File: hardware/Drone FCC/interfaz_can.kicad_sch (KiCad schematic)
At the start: 14 parts, among them J801 CAN 1 Connector 1, J803 CAN 2 Connector 1, U801 SN65HVD230, U802 SN65HVD230

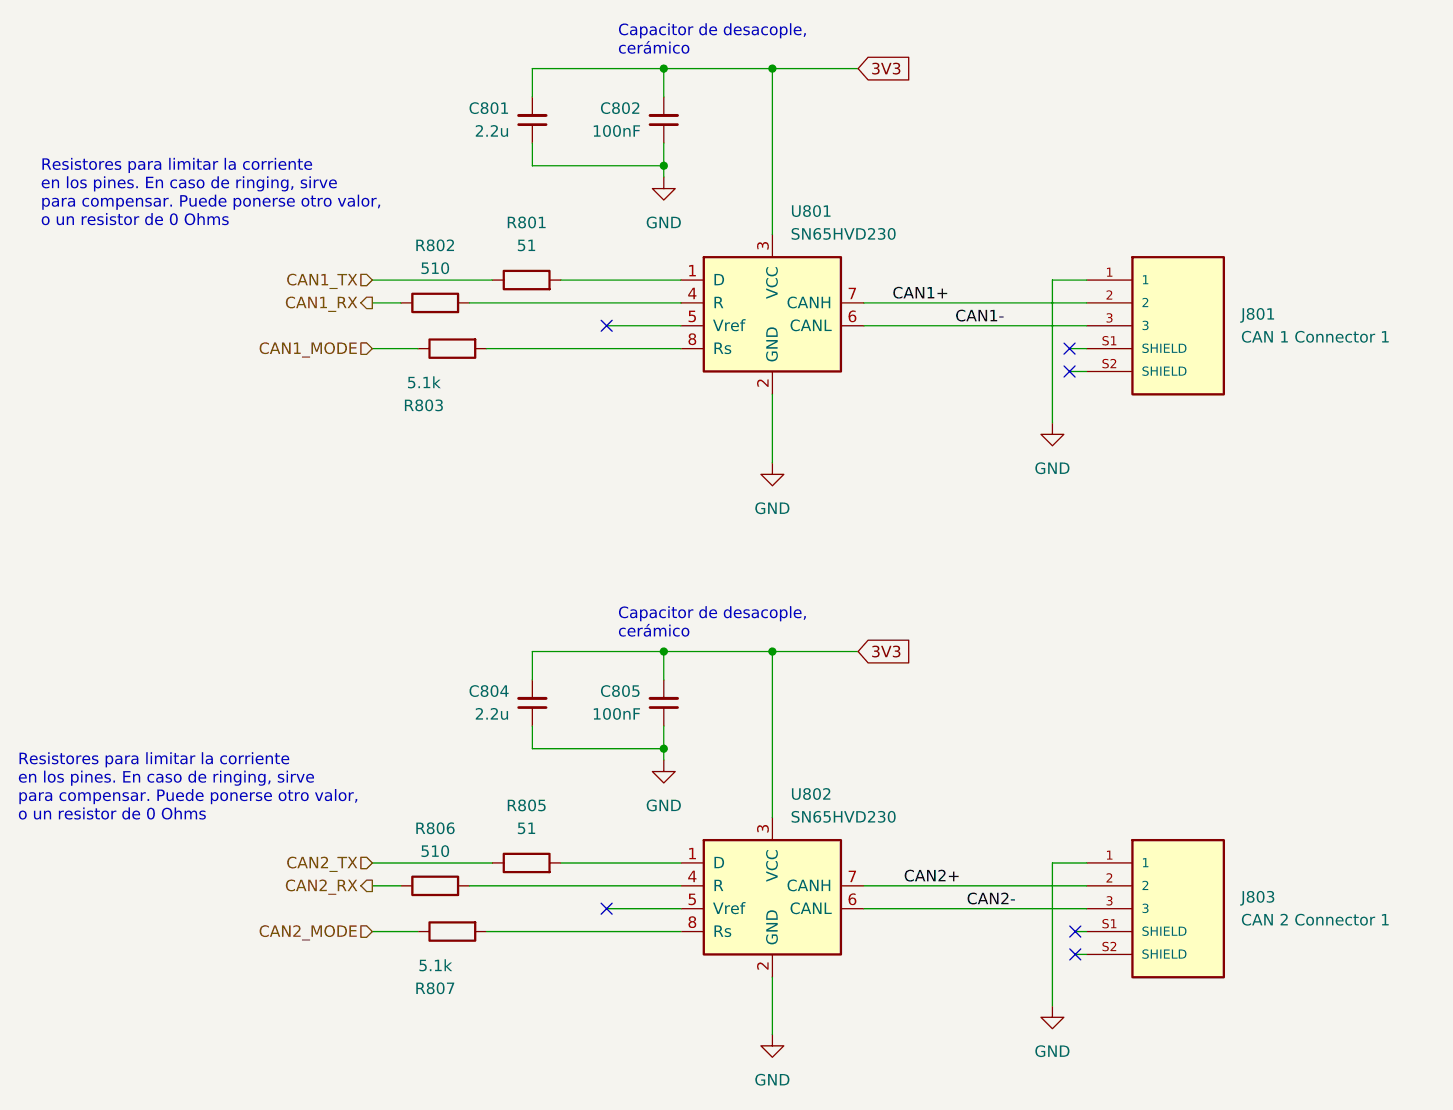
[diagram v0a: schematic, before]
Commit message: re enumeation of componentes
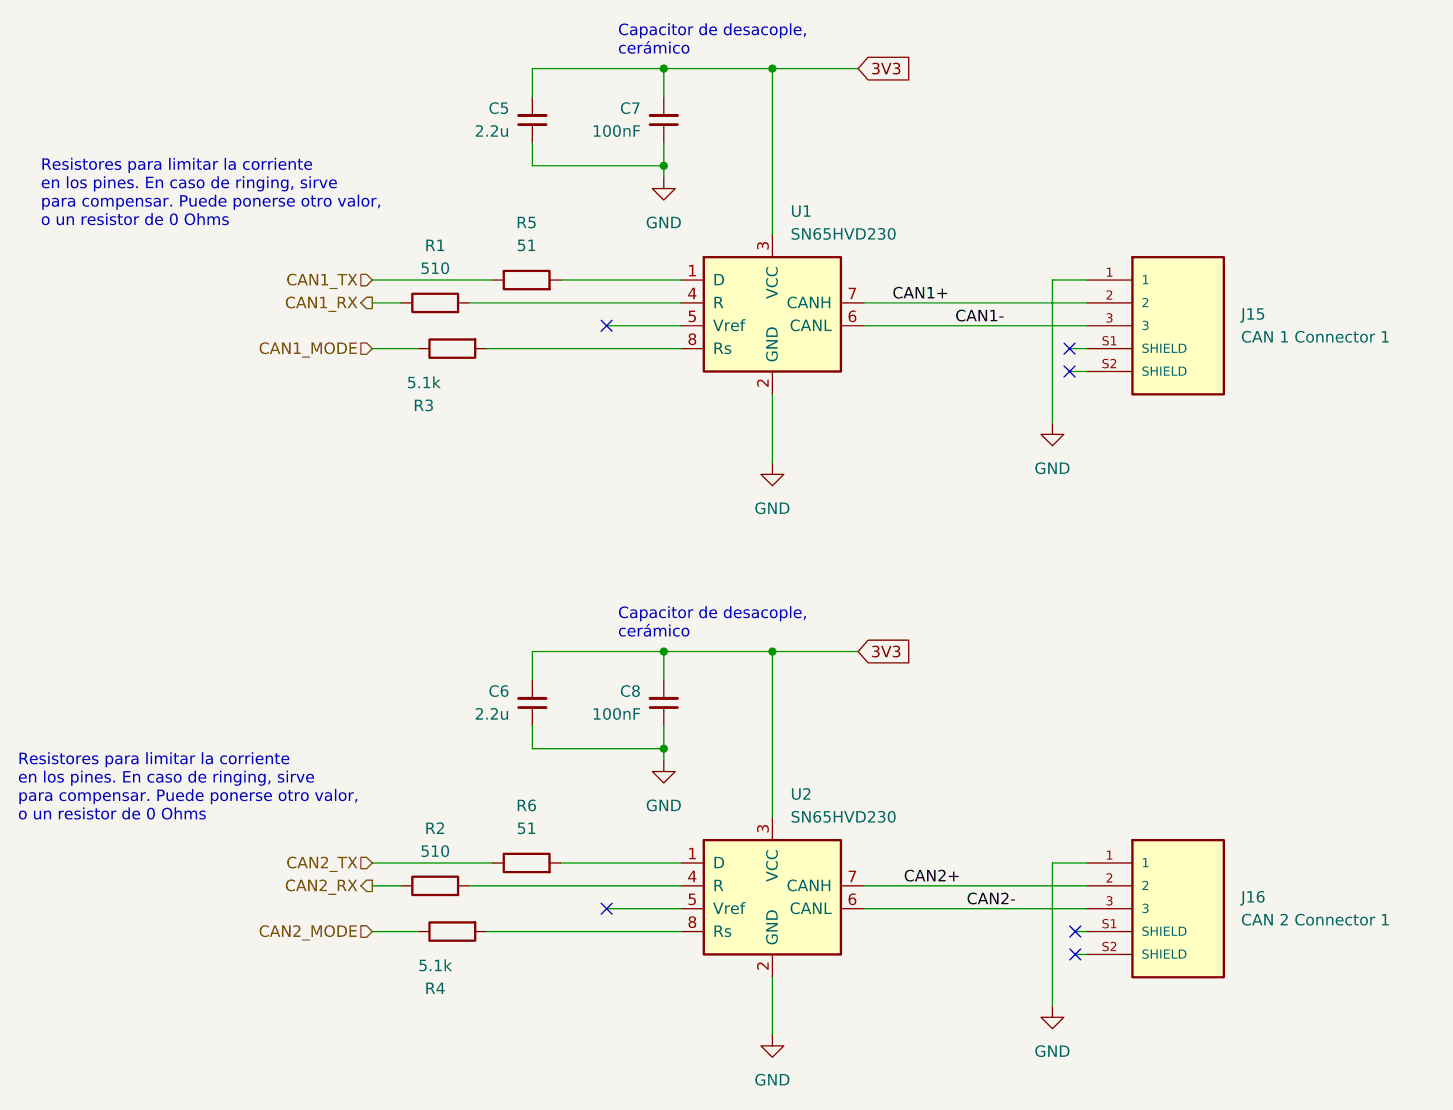
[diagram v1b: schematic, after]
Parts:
- renumbered C801 to C5, C804 to C6, C802 to C7, C805 to C8, J801 to J15, J803 to J16, R802 to R1, R806 to R2, R803 to R3, R807 to R4, R801 to R5, R805 to R6, U801 to U1, U802 to U2
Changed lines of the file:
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@@
   (symbol (lib_id "Device:R") (at 118.11 114.3 90) (unit 1)
     (in_bom yes) (on_board yes) (fields_autoplaced)
-    (property "Reference" "R805" (id 0) (at 118.11 107.95 90))
+    (property "Reference" "R6" (id 0) (at 118.11 107.95 90))
     (property "Value" "51" (id 1) (at 118.11 110.49 90))
     (property "Footprint" "Resistor_SMD:R_0402_1005Metric_Pad0.72x0.64mm_HandSolder" (id 2) (at 118.11 116.078 90)
@@
   (symbol (lib_id "Interface_CAN_LIN:SN65HVD230") (at 145.415 52.07 0) (unit 1)
     (in_bom yes) (on_board yes) (fields_autoplaced)
-    (property "Reference" "U801" (id 0) (at 147.4344 41.91 0)
+    (property "Reference" "U1" (id 0) (at 147.4344 41.91 0)
       (effects (font (size 1.27 1.27)) (justify left))
     )
@@
   (symbol (lib_name "GND_2") (lib_id "power:GND") (at 176.53 130.175 0) (unit 1)
     (in_bom yes) (on_board yes) (fields_autoplaced)
-    (property "Reference" "#PWR0104" (id 0) (at 176.53 136.525 0)
+    (property "Reference" "#PWR024" (id 0) (at 176.53 136.525 0)
       (effects (font (size 1.27 1.27)) hide)
     )
@@
   (symbol (lib_id "DF13A-3P-1.25H(21):HRS_DF13A-3P-1.25H(21)") (at 189.23 137.16 0) (unit 1)
     (in_bom yes) (on_board yes) (fields_autoplaced)
-    (property "Reference" "J803" (id 0) (at 197.485 118.1099 0)
+    (property "Reference" "J16" (id 0) (at 197.485 118.1099 0)
       (effects (font (size 1.27 1.27)) (justify left))
     )
@@
   (symbol (lib_id "Interface_CAN_LIN:SN65HVD230") (at 145.415 116.84 0) (unit 1)
     (in_bom yes) (on_board yes) (fields_autoplaced)
-    (property "Reference" "U802" (id 0) (at 147.4344 106.68 0)
+    (property "Reference" "U2" (id 0) (at 147.4344 106.68 0)
       (effects (font (size 1.27 1.27)) (justify left))
     )
@@
   (symbol (lib_id "Device:R") (at 107.95 52.07 90) (unit 1)
     (in_bom yes) (on_board yes) (fields_autoplaced)
-    (property "Reference" "R802" (id 0) (at 107.95 45.72 90))
+    (property "Reference" "R1" (id 0) (at 107.95 45.72 90))
     (property "Value" "510" (id 1) (at 107.95 48.26 90))
     (property "Footprint" "Resistor_SMD:R_0402_1005Metric_Pad0.72x0.64mm_HandSolder" (id 2) (at 107.95 53.848 90)
@@
   (symbol (lib_id "Device:C_Small") (at 118.745 96.52 0) (mirror x) (unit 1)
     (in_bom yes) (on_board yes) (fields_autoplaced)
-    (property "Reference" "C804" (id 0) (at 116.205 95.2435 0)
+    (property "Reference" "C6" (id 0) (at 116.205 95.2435 0)
       (effects (font (size 1.27 1.27)) (justify right))
     )
@@
   (symbol (lib_id "Device:C_Small") (at 133.35 31.75 0) (mirror x) (unit 1)
     (in_bom yes) (on_board yes) (fields_autoplaced)
-    (property "Reference" "C802" (id 0) (at 130.81 30.4735 0)
+    (property "Reference" "C7" (id 0) (at 130.81 30.4735 0)
       (effects (font (size 1.27 1.27)) (justify right))
     )
@@
   (symbol (lib_id "Device:R") (at 109.855 121.92 90) (mirror x) (unit 1)
     (in_bom yes) (on_board yes)
-    (property "Reference" "R807" (id 0) (at 107.95 128.27 90))
+    (property "Reference" "R4" (id 0) (at 107.95 128.27 90))
     (property "Value" "5.1k" (id 1) (at 107.95 125.73 90))
     (property "Footprint" "Resistor_SMD:R_0402_1005Metric_Pad0.72x0.64mm_HandSolder" (id 2) (at 109.855 120.142 90)
@@
   (symbol (lib_id "Device:C_Small") (at 118.745 31.75 0) (mirror x) (unit 1)
     (in_bom yes) (on_board yes) (fields_autoplaced)
-    (property "Reference" "C801" (id 0) (at 116.205 30.4735 0)
+    (property "Reference" "C5" (id 0) (at 116.205 30.4735 0)
       (effects (font (size 1.27 1.27)) (justify right))
     )
@@
   (symbol (lib_id "Device:R") (at 109.855 57.15 90) (mirror x) (unit 1)
     (in_bom yes) (on_board yes)
-    (property "Reference" "R803" (id 0) (at 106.68 63.5 90))
+    (property "Reference" "R3" (id 0) (at 106.68 63.5 90))
     (property "Value" "5.1k" (id 1) (at 106.68 60.96 90))
     (property "Footprint" "Resistor_SMD:R_0402_1005Metric_Pad0.72x0.64mm_HandSolder" (id 2) (at 109.855 55.372 90)
@@
   (symbol (lib_id "Device:R") (at 107.95 116.84 90) (unit 1)
     (in_bom yes) (on_board yes) (fields_autoplaced)
-    (property "Reference" "R806" (id 0) (at 107.95 110.49 90))
+    (property "Reference" "R2" (id 0) (at 107.95 110.49 90))
     (property "Value" "510" (id 1) (at 107.95 113.03 90))
     (property "Footprint" "Resistor_SMD:R_0402_1005Metric_Pad0.72x0.64mm_HandSolder" (id 2) (at 107.95 118.618 90)
@@
   (symbol (lib_id "power:GND") (at 145.415 69.85 0) (unit 1)
     (in_bom yes) (on_board yes) (fields_autoplaced)
-    (property "Reference" "#PWR0102" (id 0) (at 145.415 76.2 0)
+    (property "Reference" "#PWR021" (id 0) (at 145.415 76.2 0)
       (effects (font (size 1.27 1.27)) hide)
     )
@@
   (symbol (lib_id "Device:C_Small") (at 133.35 96.52 0) (mirror x) (unit 1)
     (in_bom yes) (on_board yes) (fields_autoplaced)
-    (property "Reference" "C805" (id 0) (at 130.81 95.2435 0)
+    (property "Reference" "C8" (id 0) (at 130.81 95.2435 0)
       (effects (font (size 1.27 1.27)) (justify right))
     )
@@
   (symbol (lib_name "GND_2") (lib_id "power:GND") (at 176.53 65.405 0) (unit 1)
     (in_bom yes) (on_board yes) (fields_autoplaced)
-    (property "Reference" "#PWR0101" (id 0) (at 176.53 71.755 0)
+    (property "Reference" "#PWR023" (id 0) (at 176.53 71.755 0)
       (effects (font (size 1.27 1.27)) hide)
     )
@@
   (symbol (lib_id "DF13A-3P-1.25H(21):HRS_DF13A-3P-1.25H(21)") (at 189.23 72.39 0) (unit 1)
     (in_bom yes) (on_board yes) (fields_autoplaced)
-    (property "Reference" "J801" (id 0) (at 197.485 53.3399 0)
+    (property "Reference" "J15" (id 0) (at 197.485 53.3399 0)
       (effects (font (size 1.27 1.27)) (justify left))
     )
@@
   (symbol (lib_id "power:GND") (at 133.35 38.1 0) (unit 1)
     (in_bom yes) (on_board yes) (fields_autoplaced)
-    (property "Reference" "#PWR0122" (id 0) (at 133.35 44.45 0)
+    (property "Reference" "#PWR019" (id 0) (at 133.35 44.45 0)
       (effects (font (size 1.27 1.27)) hide)
     )
@@
   (symbol (lib_id "power:GND") (at 145.415 133.35 0) (unit 1)
     (in_bom yes) (on_board yes) (fields_autoplaced)
-    (property "Reference" "#PWR0136" (id 0) (at 145.415 139.7 0)
+    (property "Reference" "#PWR022" (id 0) (at 145.415 139.7 0)
       (effects (font (size 1.27 1.27)) hide)
     )
@@
   (symbol (lib_id "Device:R") (at 118.11 49.53 90) (unit 1)
     (in_bom yes) (on_board yes) (fields_autoplaced)
-    (property "Reference" "R801" (id 0) (at 118.11 43.18 90))
+    (property "Reference" "R5" (id 0) (at 118.11 43.18 90))
     (property "Value" "51" (id 1) (at 118.11 45.72 90))
     (property "Footprint" "Resistor_SMD:R_0402_1005Metric_Pad0.72x0.64mm_HandSolder" (id 2) (at 118.11 51.308 90)
@@
   (symbol (lib_id "power:GND") (at 133.35 102.87 0) (unit 1)
     (in_bom yes) (on_board yes) (fields_autoplaced)
-    (property "Reference" "#PWR0133" (id 0) (at 133.35 109.22 0)
-      (effects (font (size 1.27 1.27)) hide)
-    )
+    (property "Reference" "#PWR020" (id 0) (at 133.35 109.22 0)
+      (effects (font (size 1.27 1.27)) hide)
+    )
